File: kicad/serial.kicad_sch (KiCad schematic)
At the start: 3 parts, among them U119 8274, U165 PAL16L8, U82 74LS00

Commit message: update kicad project
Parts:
- removed U165: PAL16L8, Package_DIP:DIP-20_W7.62mm, symbol Logic_Programmable:PAL16L8
- U119: seq_coord (none) -> D29
- U82: seq_coord (none) -> D20; seq_silkscreen (none) -> LS00
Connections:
- net PD0: now also U119.19 (DB0)
- net PD2: now also U119.17 (DB2)
- net PD4: now also U119.15 (DB4)
- net PD5: now also U119.14 (DB5)
- net PD7: now reaches U119.12 (DB7)
- net PD6: now reaches U119.13 (DB6)
- net PD3: now reaches U119.16 (DB3)
- net PD1: now reaches U119.18 (DB1)

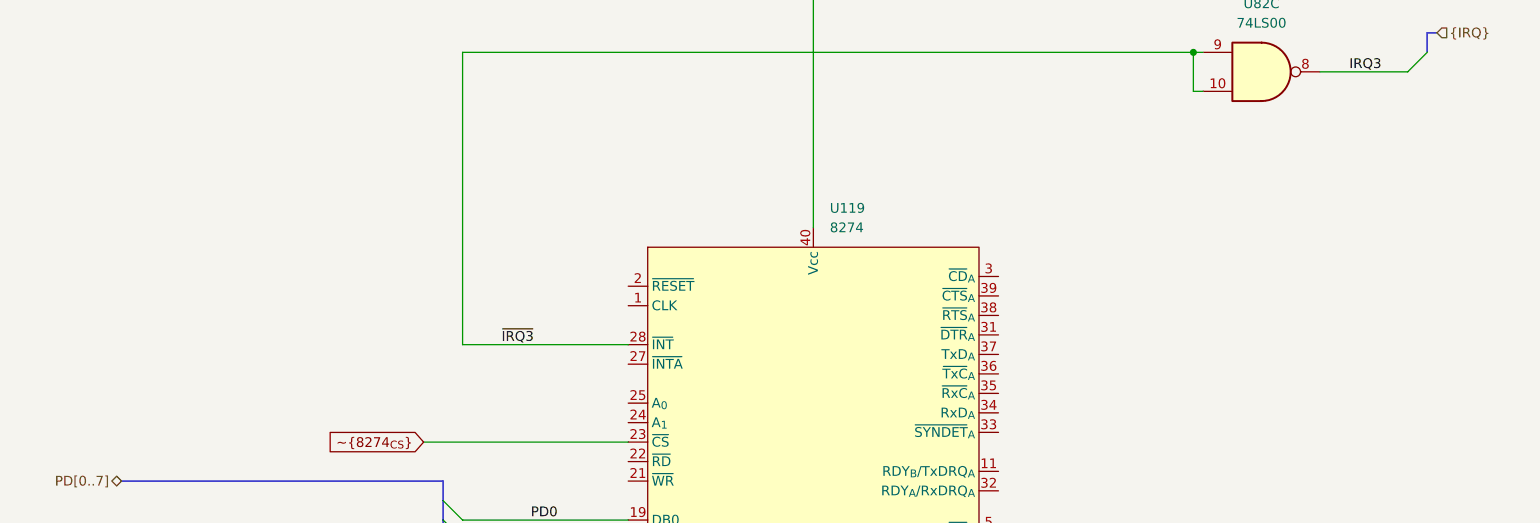
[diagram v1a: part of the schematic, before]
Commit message: Add parallel port, game port
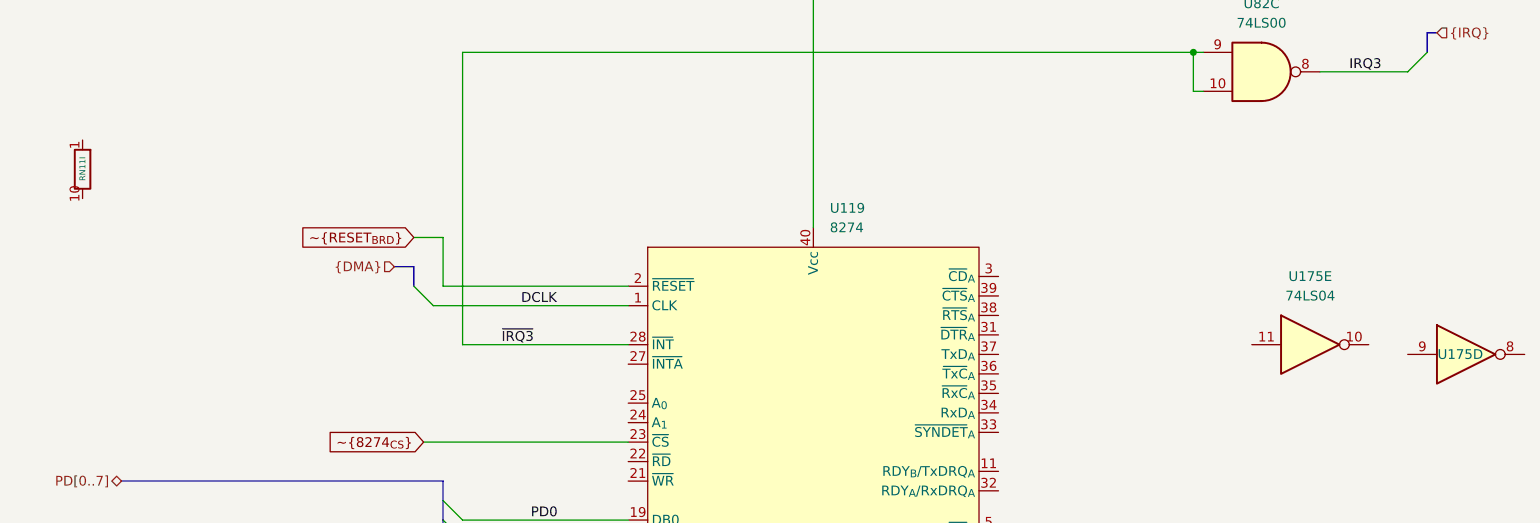
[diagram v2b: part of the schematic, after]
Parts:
- added RN11: 4.7kΩ, Resistor_THT:R_Array_SIP10, symbol Device:R_Network09_Split
- added U175: 74LS04, Package_DIP:DIP-14_W7.62mm, symbol 74xx:74LS04
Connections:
- net DCLK: now reaches U119.1 (CLK)
- net ~{RESET_{BRD}}: now reaches U119.2 (~{RESET})
